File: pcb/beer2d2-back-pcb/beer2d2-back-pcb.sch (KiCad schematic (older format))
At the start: 38 parts, among them IC1 74HC238, IC2 TLC5971, IC3 FT230X, IC4 LM1117, IC5 ATMEGA328P, J1 USB, J2 PSI1, J3 PSI2, J4 RGB1, J5 RGB2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

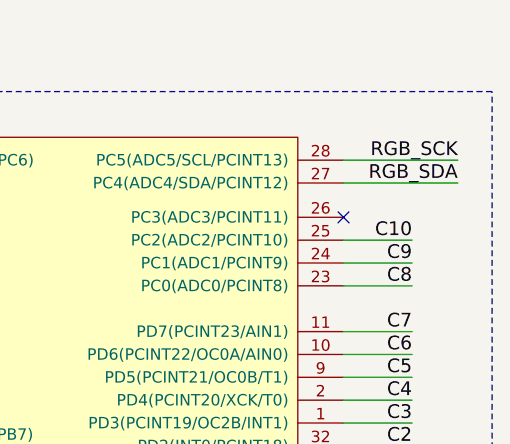
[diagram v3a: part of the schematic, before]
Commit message: layout back board copper
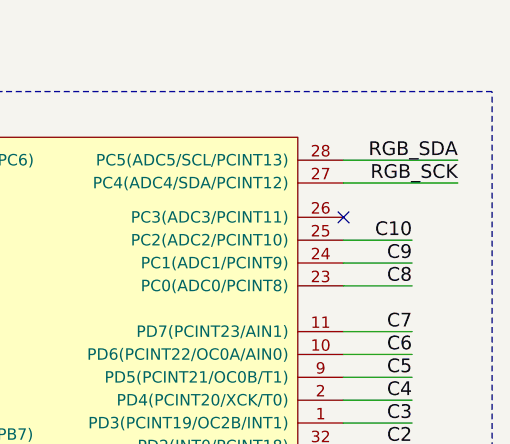
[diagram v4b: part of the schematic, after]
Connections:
- net RGB_SCK: now also IC5.27 (PC4(ADC4/SDA/PCINT12)); no longer IC5.28 (PC5(ADC5/SCL/PCINT13))
- net RGB_SDA: now also IC5.28 (PC5(ADC5/SCL/PCINT13)); no longer IC5.27 (PC4(ADC4/SDA/PCINT12))
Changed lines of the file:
@@
 Text Label 6950 1350 0    60   ~ 0
 AVR_RST
+Text Label 9900 1450 2    60   ~ 0
+RGB_SCK
 Text Label 9900 1350 2    60   ~ 0
-RGB_SCK
-Text Label 9900 1450 2    60   ~ 0
 RGB_SDA
 NoConn ~ 9400 1600

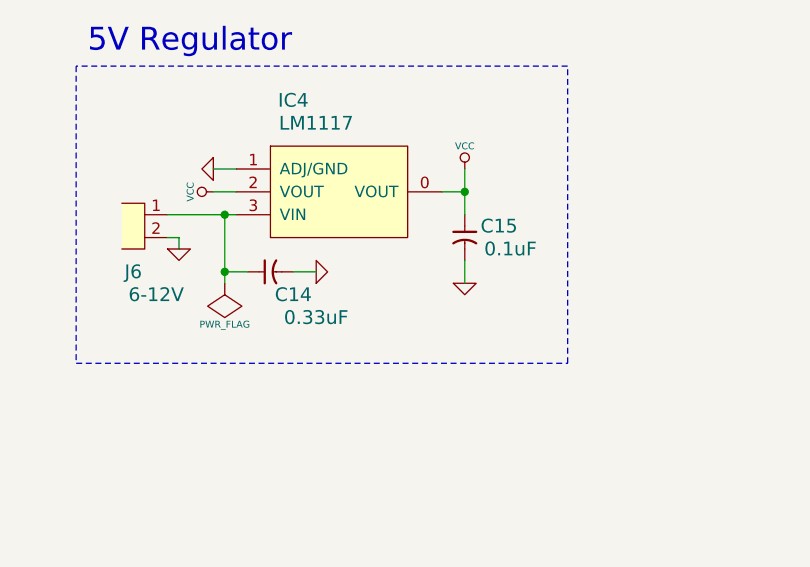
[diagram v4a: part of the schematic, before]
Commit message: fix voltage regulator cap values and footprints
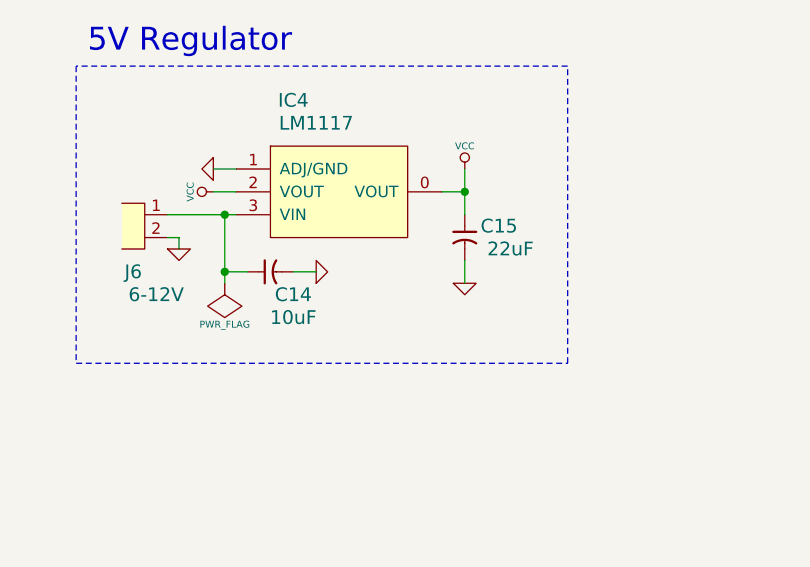
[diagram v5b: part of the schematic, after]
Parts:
- C14: value 0.33uF -> 10uF
- C15: value 0.1uF -> 22uF
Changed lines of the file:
@@
 P 7500 5950
 F 0 "C14" H 7600 5850 60  0000 C CNN
-F 1 "0.33uF" H 7700 5750 60  0000 C CNN
+F 1 "10uF" H 7600 5750 60  0000 C CNN
 F 2 "" H 7500 5950 60  0001 C CNN
 F 3 "" H 7500 5950 60  0001 C CNN
@@
 P 8350 5800
 F 0 "C15" V 8300 5950 60  0000 C CNN
-F 1 "0.1uF" V 8400 6000 60  0000 C CNN
+F 1 "22uF" V 8400 6000 60  0000 C CNN
 F 2 "" H 8350 5800 60  0001 C CNN
 F 3 "" H 8350 5800 60  0001 C CNN
